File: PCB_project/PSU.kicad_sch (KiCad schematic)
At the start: 20 parts, among them IC1 TPS62142, J2 Conn_01x02, U10 AMS1117-3.3

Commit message: Schematic updated
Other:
- title: KP-PTR -> KP-PTR project - PTR_mini
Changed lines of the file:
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@@
 	(paper "A4")
 	(title_block
-		(title "KP-PTR")
-		(date "2023-12-10")
-		(rev "1.1")
+		(title "KP-PTR project - PTR_mini")
+		(date "2026-09-17")
+		(rev "1.0")
 		(company "Polskie Towarzystwo Rakietowe")
 		(comment 1 "bartekM, FlyingBanana, Kretu, Red Labs, Stachu M, U.S. air force i inni")

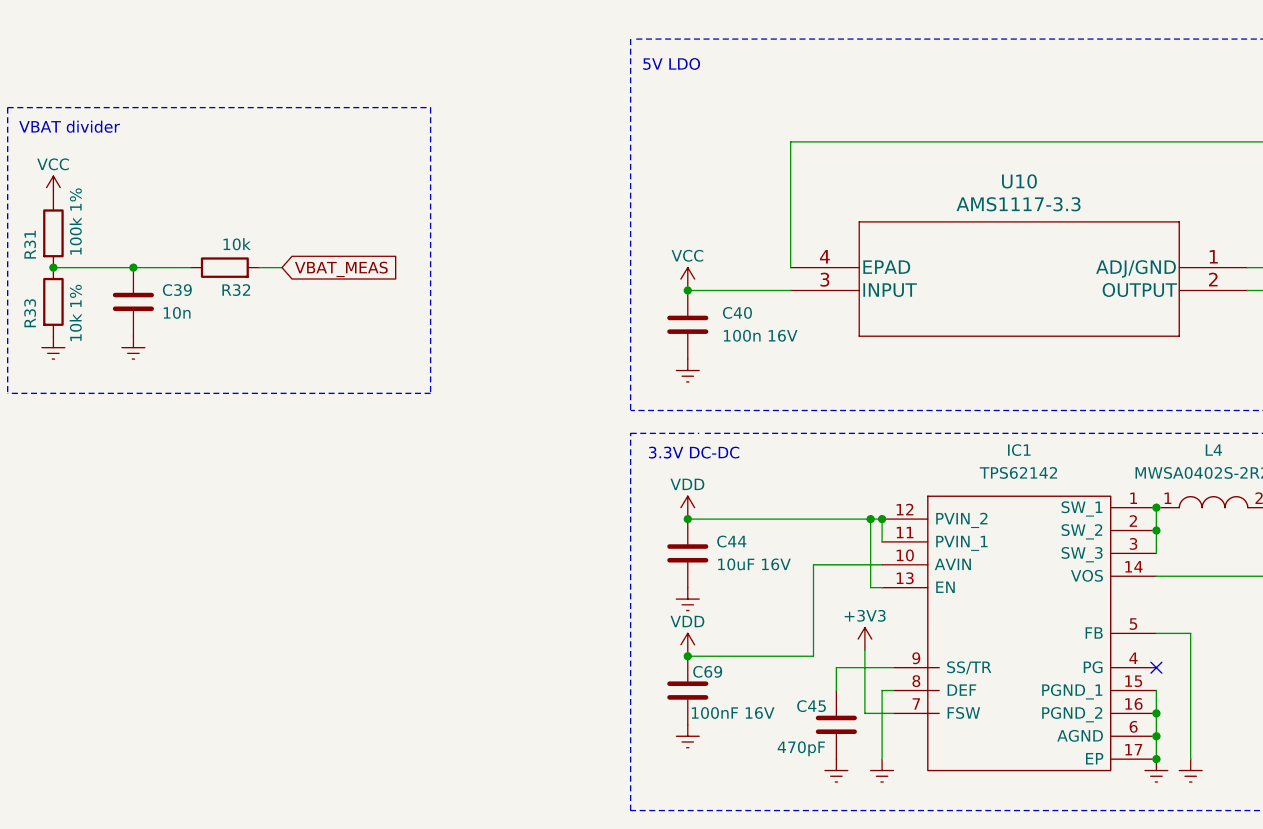
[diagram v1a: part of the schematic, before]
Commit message: + USB connector changed to SMD
+ igniters connectors changed to single 6 pin connector
+ buzzer selected
+ crystal changed to TCXO (experimental)
+ JLC production files generated
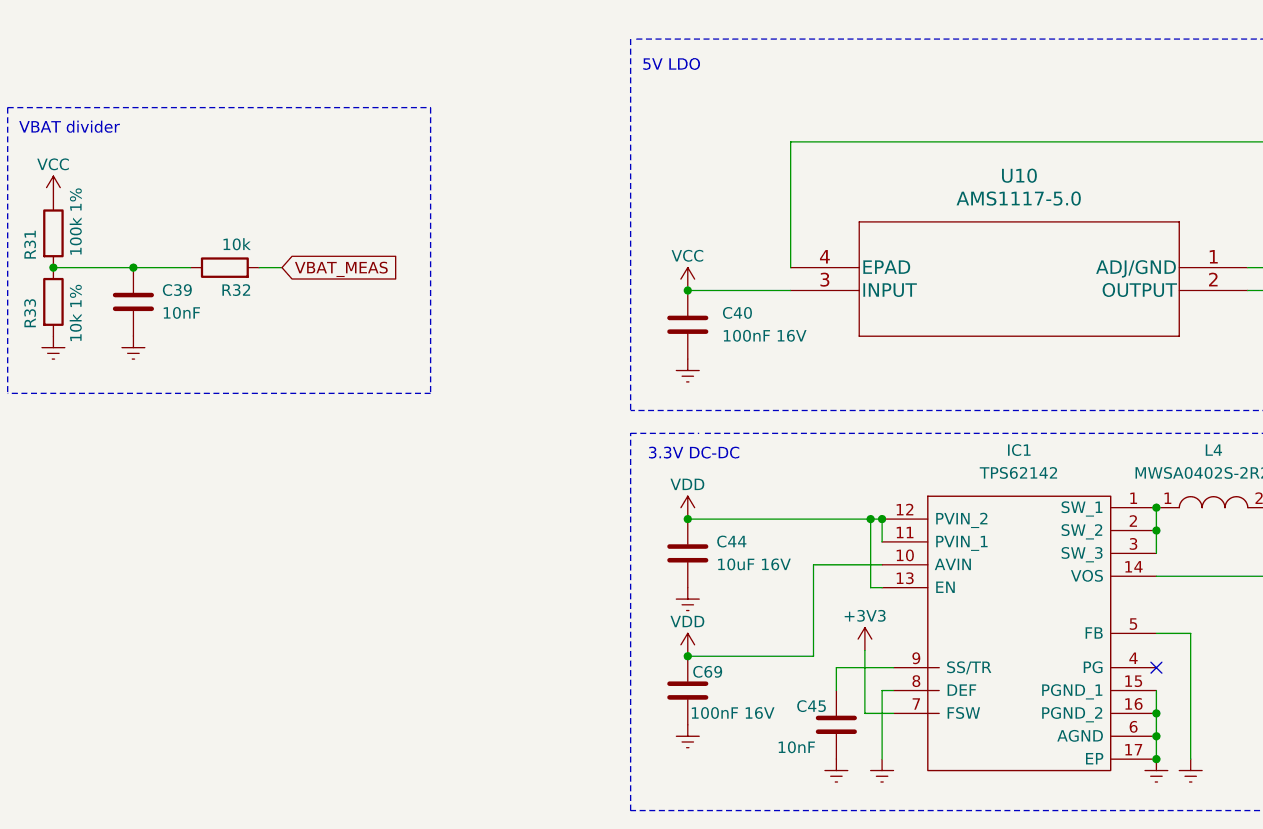
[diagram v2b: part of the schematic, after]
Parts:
- C39: value 10n -> 10nF
- C40: value 100n 16V -> 100nF 16V
- C41: footprint Capacitor_SMD:C_0402_1005Metric -> Capacitor_SMD:C_0603_1608Metric
- C45: value 470pF -> 10nF
- U10: value AMS1117-3.3 -> AMS1117-5.0
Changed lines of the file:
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@@
 			)
 		)
-		(property "Value" "470pF"
+		(property "Value" "10nF"
 			(at 112.776 151.13 0)
 			(show_name no)
@@
 		(fields_autoplaced yes)
 		(property "Reference" "U10"
-			(at 139.7 88.265 0)
+			(at 139.7 87.63 0)
 			(show_name no)
 			(do_not_autoplace no)
@@
 			)
 		)
-		(property "Value" "AMS1117-3.3"
-			(at 139.7 90.805 0)
+		(property "Value" "AMS1117-5.0"
+			(at 139.7 90.17 0)
 			(show_name no)
 			(do_not_autoplace no)
@@
 			)
 		)
-		(property "Footprint" "Capacitor_SMD:C_0402_1005Metric"
+		(property "Footprint" "Capacitor_SMD:C_0603_1608Metric"
 			(at 181.9148 107.95 0)
 			(hide yes)
@@
 			)
 		)
-		(property "Value" "100n 16V"
+		(property "Value" "100nF 16V"
 			(at 106.68 105.4099 0)
 			(show_name no)
@@
 			)
 		)
-		(property "Value" "10n"
+		(property "Value" "10nF"
 			(at 44.45 102.8699 0)
 			(show_name no)

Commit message: + LDO replaced with better one (lower voltage drop)
+ Vbat meas circuit should be now more stable
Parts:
- C39: value 10nF -> 1uF
- R32: value 10k -> 22R
- U10: value AMS1117-5.0 -> LDL1117S50R
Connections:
- net VBAT_MEAS: now also C39.1
- net at R31.2, R32.1, R33.1: no longer C39.1
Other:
- moved on the sheet: C39, R32
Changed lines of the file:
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@@
 	)
 	(junction
-		(at 41.275 97.79)
+		(at 189.23 132.08)
 		(diameter 0)
 		(color 0 0 0 0)
 	)
 	(junction
-		(at 189.23 132.08)
+		(at 102.87 140.97)
 		(diameter 0)
 		(color 0 0 0 0)
 	)
 	(junction
-		(at 102.87 140.97)
+		(at 32.385 97.79)
 		(diameter 0)
 		(color 0 0 0 0)
@@
 	)
 	(junction
+		(at 48.26 97.79)
+		(diameter 0)
+		(color 0 0 0 0)
+	)
+	(junction
 		(at 222.25 124.46)
 		(diameter 0)
@@
 	)
 	(junction
-		(at 32.385 97.79)
-		(diameter 0)
-		(color 0 0 0 0)
-	)
-	(junction
 		(at 66.675 44.45)
 		(diameter 0)
@@
 	(wire
 		(pts
-			(xy 55.245 97.79) (xy 57.785 97.79)
+			(xy 45.72 97.79) (xy 48.26 97.79)
 		)
 		(stroke
@@
 	(wire
 		(pts
-			(xy 32.385 97.79) (xy 41.275 97.79)
+			(xy 32.385 97.79) (xy 38.1 97.79)
 		)
 		(stroke
@@
 		)
 	)
-	(wire
-		(pts
-			(xy 41.275 97.79) (xy 47.625 97.79)
-		)
-		(stroke
-			(width 0)
-			(type default)
-		)
-	)
 	(polyline
 		(pts
@@
 	(wire
 		(pts
+			(xy 48.26 97.79) (xy 57.785 97.79)
+		)
+		(stroke
+			(width 0)
+			(type default)
+		)
+	)
+	(wire
+		(pts
 			(xy 102.87 125.73) (xy 123.19 125.73)
 		)
@@
 	(symbol
 		(lib_id "Device:R")
-		(at 51.435 97.79 90)
+		(at 41.91 97.79 90)
 		(unit 1)
 		(body_style 1)
@@
 		(dnp no)
 		(property "Reference" "R32"
-			(at 52.705 100.33 90)
+			(at 43.18 100.33 90)
 			(show_name no)
 			(do_not_autoplace no)
@@
 			)
 		)
-		(property "Value" "10k"
-			(at 52.705 95.25 90)
+		(property "Value" "22R"
+			(at 42.037 97.79 90)
 			(show_name no)
 			(do_not_autoplace no)
@@
 		)
 		(property "Footprint" "Resistor_SMD:R_0402_1005Metric"
-			(at 51.435 99.568 90)
+			(at 41.91 99.568 90)
 			(hide yes)
 			(show_name no)
@@
 		)
 		(property "Datasheet" ""
-			(at 51.435 97.79 0)
+			(at 41.91 97.79 0)
 			(hide yes)
 			(show_name no)
@@
 		)
 		(property "Description" ""
-			(at 51.435 97.79 0)
+			(at 41.91 97.79 0)
 			(show_name no)
 			(do_not_autoplace no)
@@
 			)
 		)
-		(property "Value" "AMS1117-5.0"
+		(property "Value" "LDL1117S50R"
 			(at 139.7 90.17 0)
 			(show_name no)
@@
 	(symbol
 		(lib_id "power:Earth")
-		(at 41.275 105.41 0)
+		(at 48.26 105.41 0)
 		(unit 1)
 		(body_style 1)
@@
 		(fields_autoplaced yes)
 		(property "Reference" "#PWR0114"
-			(at 41.275 111.76 0)
+			(at 48.26 111.76 0)
 			(hide yes)
 			(show_name no)
@@
 		)
 		(property "Value" "Earth"
-			(at 41.275 109.22 0)
+			(at 48.26 109.22 0)
 			(hide yes)
 			(show_name no)
@@
 		)
 		(property "Footprint" ""
-			(at 41.275 105.41 0)
+			(at 48.26 105.41 0)
 			(hide yes)
 			(show_name no)
@@
 		)
 		(property "Datasheet" ""
-			(at 41.275 105.41 0)
+			(at 48.26 105.41 0)
 			(hide yes)
 			(show_name no)
@@
 		)
 		(property "Description" ""
-			(at 41.275 105.41 0)
+			(at 48.26 105.41 0)
 			(show_name no)
 			(do_not_autoplace no)
@@
 	(symbol
 		(lib_id "Device:C")
-		(at 41.275 101.6 0)
+		(at 48.26 101.6 0)
 		(unit 1)
 		(body_style 1)
@@
 		(fields_autoplaced yes)
 		(property "Reference" "C39"
-			(at 44.45 100.3299 0)
+			(at 51.435 100.3299 0)
 			(show_name no)
 			(do_not_autoplace no)
@@
 			)
 		)
-		(property "Value" "10nF"
-			(at 44.45 102.8699 0)
+		(property "Value" "1uF"
+			(at 51.435 102.8699 0)
 			(show_name no)
 			(do_not_autoplace no)
@@
 		)
 		(property "Footprint" "Capacitor_SMD:C_0402_1005Metric"
-			(at 42.2402 105.41 0)
+			(at 49.2252 105.41 0)
 			(hide yes)
 			(show_name no)
@@
 		)
 		(property "Datasheet" ""
-			(at 41.275 101.6 0)
+			(at 48.26 101.6 0)
 			(hide yes)
 			(show_name no)
@@
 		)
 		(property "Description" ""
-			(at 41.275 101.6 0)
+			(at 48.26 101.6 0)
 			(show_name no)
 			(do_not_autoplace no)
